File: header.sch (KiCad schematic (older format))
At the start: 37 parts, among them J1 Conn_01x10, J2 Conn_01x08, J3 Conn_01x06, J4 Conn_01x08, Q2 Q_NMOS_GSD, Q3 Q_NMOS_GSD, Q4 Q_NMOS_GSD, SW6 SW_Push, U1 ICE40HX4K-TQ144, U20 MAX11614, U8 TXS0108EPW, U9 TXS0108EPW, Y2 ECS-3225S33-500-FN-TR

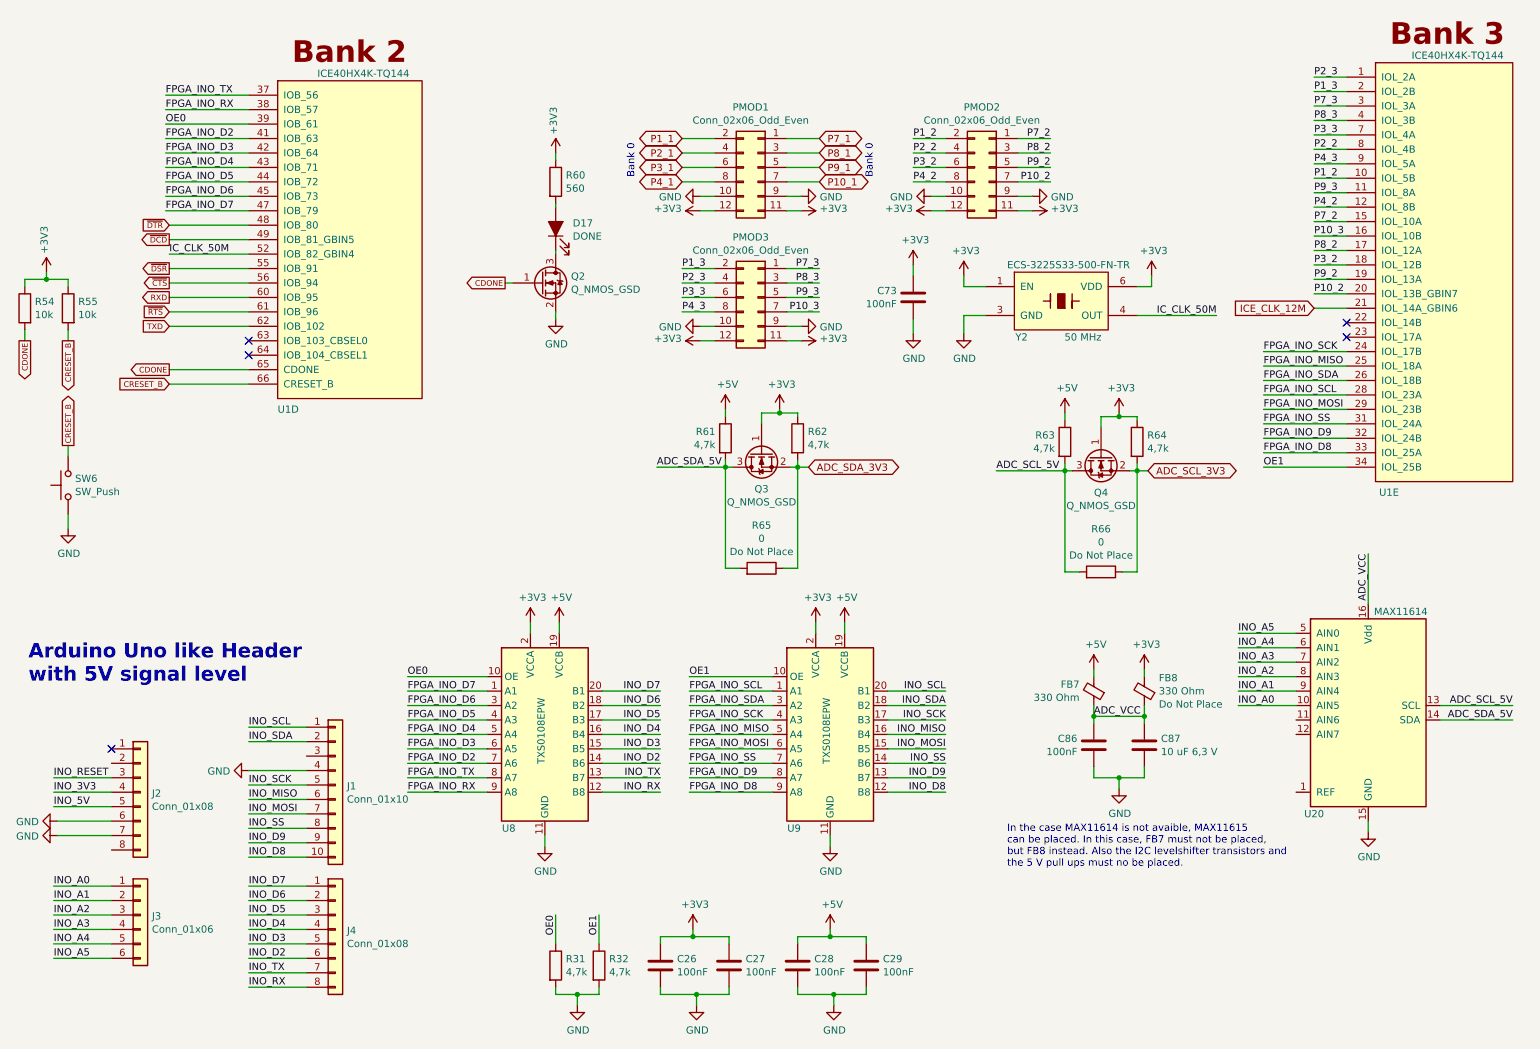
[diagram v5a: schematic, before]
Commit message: Changed power isolation to usb power to use an open drain translator for the reset signals. Continued on routing
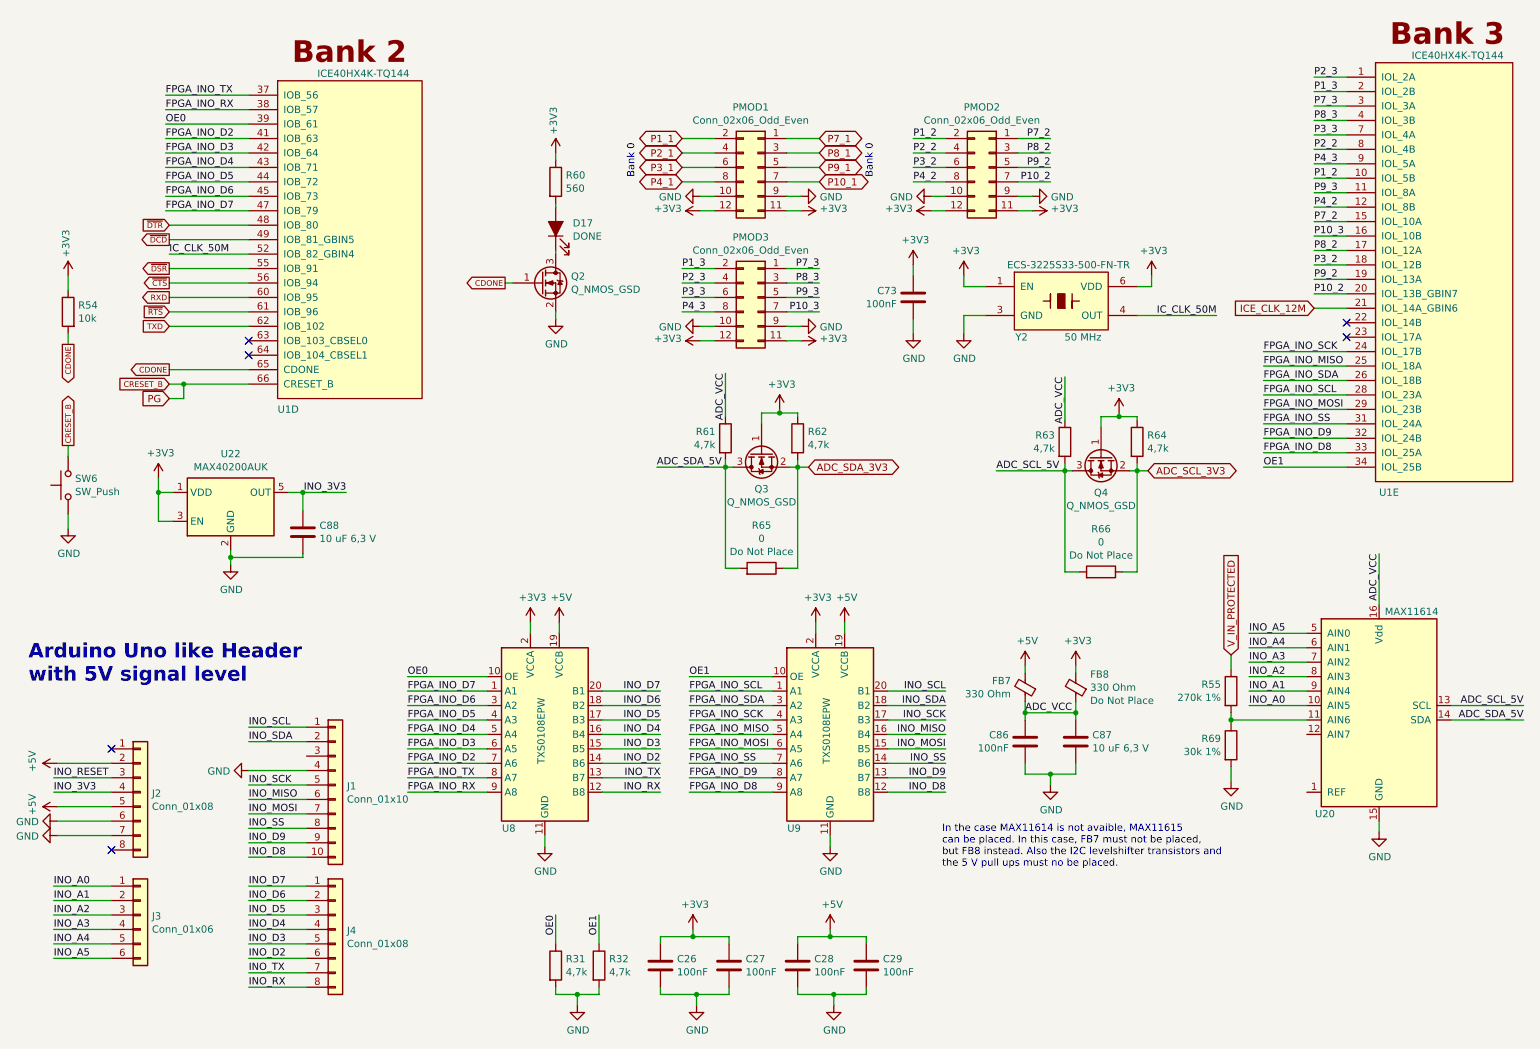
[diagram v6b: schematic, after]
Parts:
- added C88: 10 uF 6,3 V, Capacitor_SMD:C_0603_1608Metric, symbol Device:C
- added R69: 30k 1%, Resistor_SMD:R_0603_1608Metric, symbol Device:R
- added U22: MAX40200AUK, Package_TO_SOT_SMD:SOT-23-5, symbol Analog_Switch:MAX40200AUK
- R55: value 10k -> 270k 1%
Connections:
- net INO_5V is gone; now on net +5V: J2.5 (Pin_5)
- net +3V3: now also U22.1 (VDD), U22.3 (EN); no longer R55.1
- net +5V: now also J2.2 (Pin_2); no longer R61.1, R63.1
- net ADC_VCC: now also R61.1, R63.1
- net CRESET_B: no longer R55.2
- net GND: now also C88.2, R69.2, U22.2 (GND)
- net INO_3V3: now also C88.1, U22.5 (OUT)
- net at U20.11 (AIN6): now also R55.2, R69.1
- new net V_IN_PROTECTED: R55.1
- no-connect marks 5 -> 6
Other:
- moved on the sheet: C86, C87, FB7, FB8, R54, U20

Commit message: Added more BOM information, updated fpga symbol, added some more 3d models
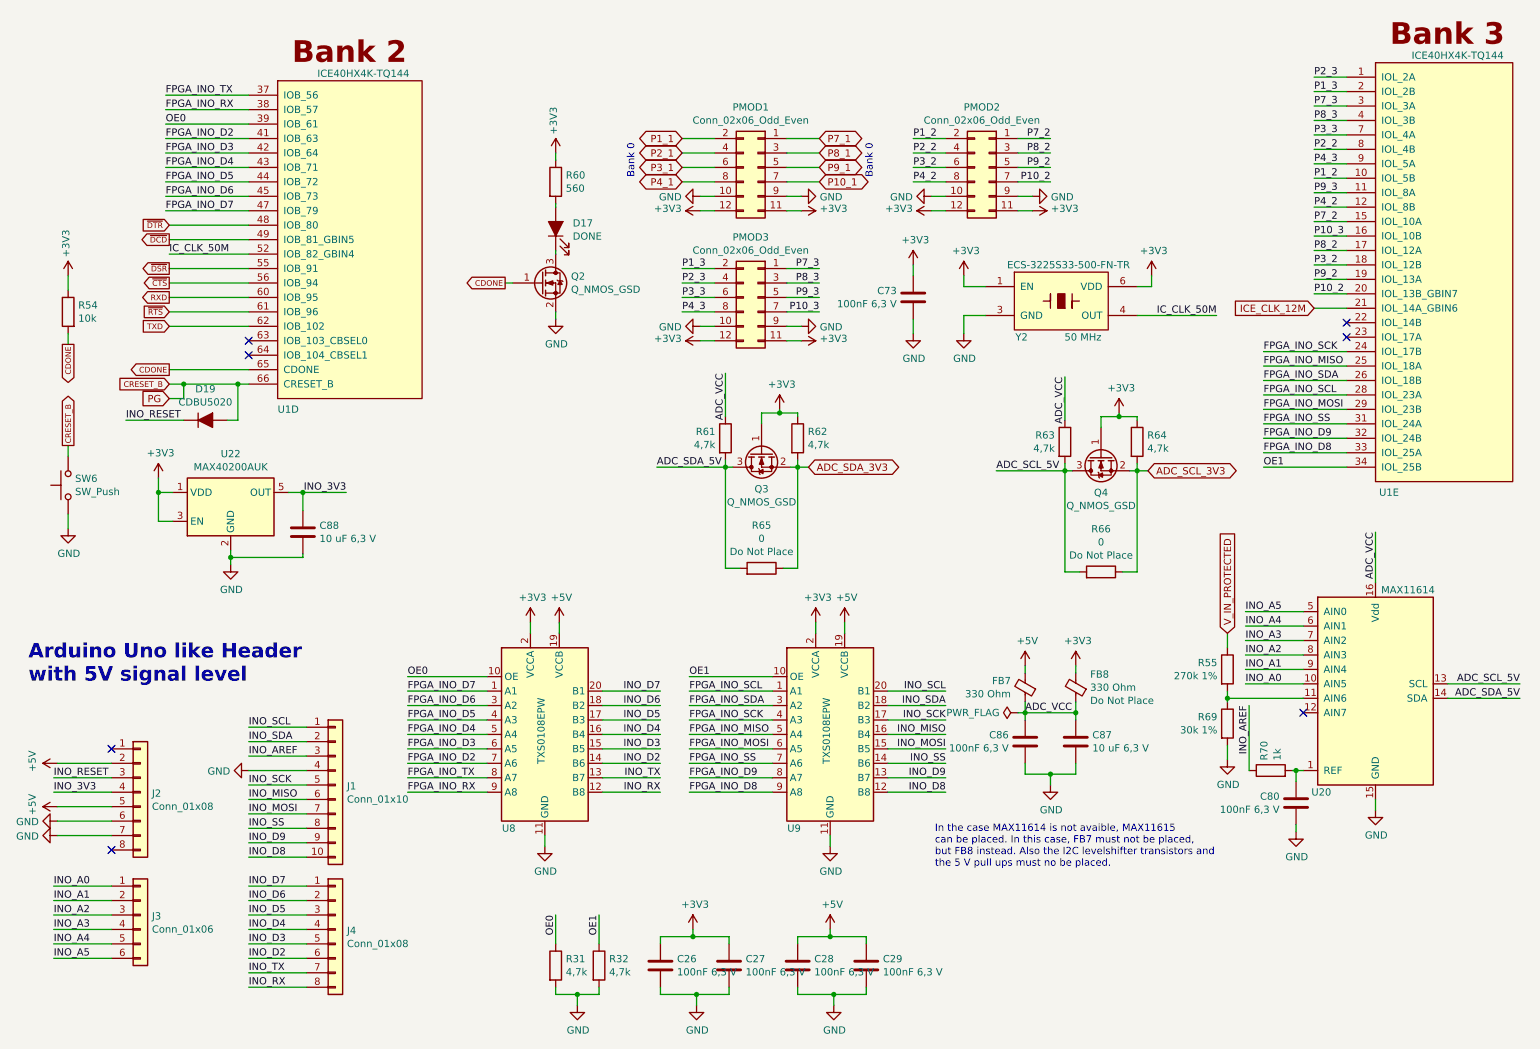
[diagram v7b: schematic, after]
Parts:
- added C80: 100nF 6,3 V, Capacitor_SMD:C_0603_1608Metric, symbol Device:C
- added D19: CDBU5020, Diode_SMD:D_0603_1608Metric, symbol Device:D_ALT
- added R70: 1k, Resistor_SMD:R_0603_1608Metric, symbol Device:R
- C26, C27, C28, C29, C73, C86: value 100nF -> 100nF 6,3 V; Description (none) -> CAP CER 0.1UF 50V X7R 0603; Digikey (none) -> 1276-1000-1-ND; Mfg Name (none) -> Samsung Electro-Mechanics; Mfg Part Num (none) -> CL10B104KB8NNNC; Spec (none) -> Any
- C87, C88: Spec (none) -> Any
- FB7, FB8, SW6, U20, U22, Y2: Spec (none) -> Spec
- Q2, Q3, Q4: Description (none) -> MOSFET N-CH 60V 310MA SOT23; Digikey (none) -> DMN65D8L-7DICT-ND; Mfg Name (none) -> Diodes Incorporated; Mfg Part Num (none) -> DMN65D8L-7; Spec (none) -> Spec
- U1: Description (none) -> IC FPGA 107 I/O 144TQFP; Digikey (none) -> 220-1572-ND; Mfg Name (none) -> Lattice Semiconductor Corporation; Mfg Part Num (none) -> ICE40HX4K-TQ144; Spec (none) -> Spec
- U8, U9: Description (none) -> IC TRNSLTR BIDIRECTIONAL 20TSSOP; Digikey (none) -> 296-23011-1-ND; Mfg Name (none) -> Texas Instruments; Mfg Part Num (none) -> TXS0108EPWR; Spec (none) -> Spec
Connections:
- net CRESET_B: now also D19.2 (A)
- net GND: now also C80.2
- net INO_RESET: now also D19.1 (K)
- net INO_AREF: now reaches J1.3 (Pin_3)
- net INO_AREF: now also R70.1
- net at U20.1 (REF): now also C80.1, R70.2
- no-connect marks 6 -> 7
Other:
- moved on the sheet: R55, R69, U20

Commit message: Corrected a few footprints
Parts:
- Y2: footprint footprints:ECS-3225S_3.2x2.5mm_footprint -> footprints:Y_ECS-3225S_3.2x2.5mm_footprint
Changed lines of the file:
@@
 F 0 "Y2" H 7675 2275 50  0000 C CNN
 F 1 "ECS-3225S33-500-FN-TR" H 8000 2775 50  0000 C CNN
-F 2 "footprints:ECS-3225S_3.2x2.5mm_footprint" H 7975 1925 50  0001 C CNN
+F 2 "footprints:Y_ECS-3225S_3.2x2.5mm_footprint" H 7975 1925 50  0001 C CNN
 F 3 "https://www.ecsxtal.com/store/pdf/ECS-3225S.pdf" H 7975 1925 50  0001 C CNN
 F 4 "ECS Inc." H 7975 2525 50  0001 C CNN "Mfg Name"
